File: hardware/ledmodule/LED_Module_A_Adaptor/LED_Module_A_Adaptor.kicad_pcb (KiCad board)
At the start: 4 copper layers, 39.9 x 20.3 mm, 8 parts, among them J1 Conn_LED_Board, J2 Conn_Cable, J3 Conn_01x04, J4 Conn_01x02

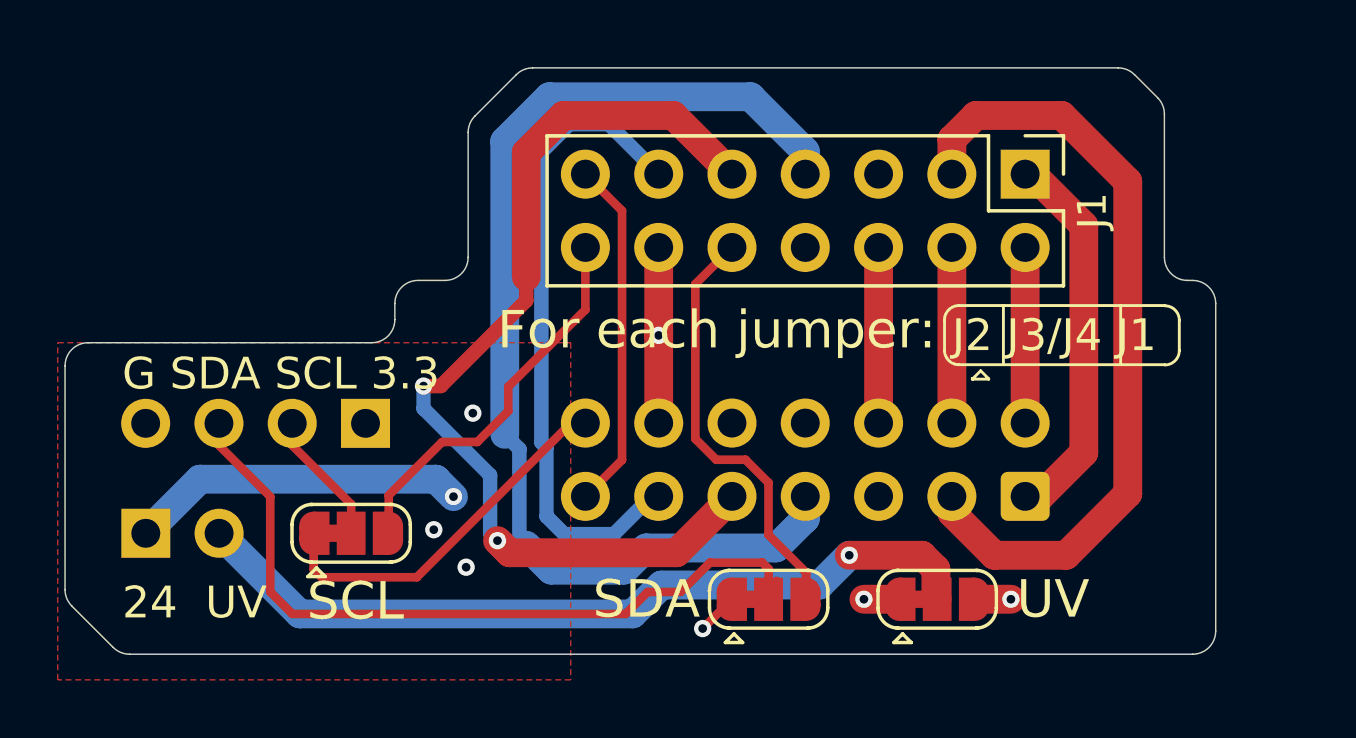
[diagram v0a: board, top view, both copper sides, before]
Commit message: v2 of the adaptor, which now should really fit into the enclosure.
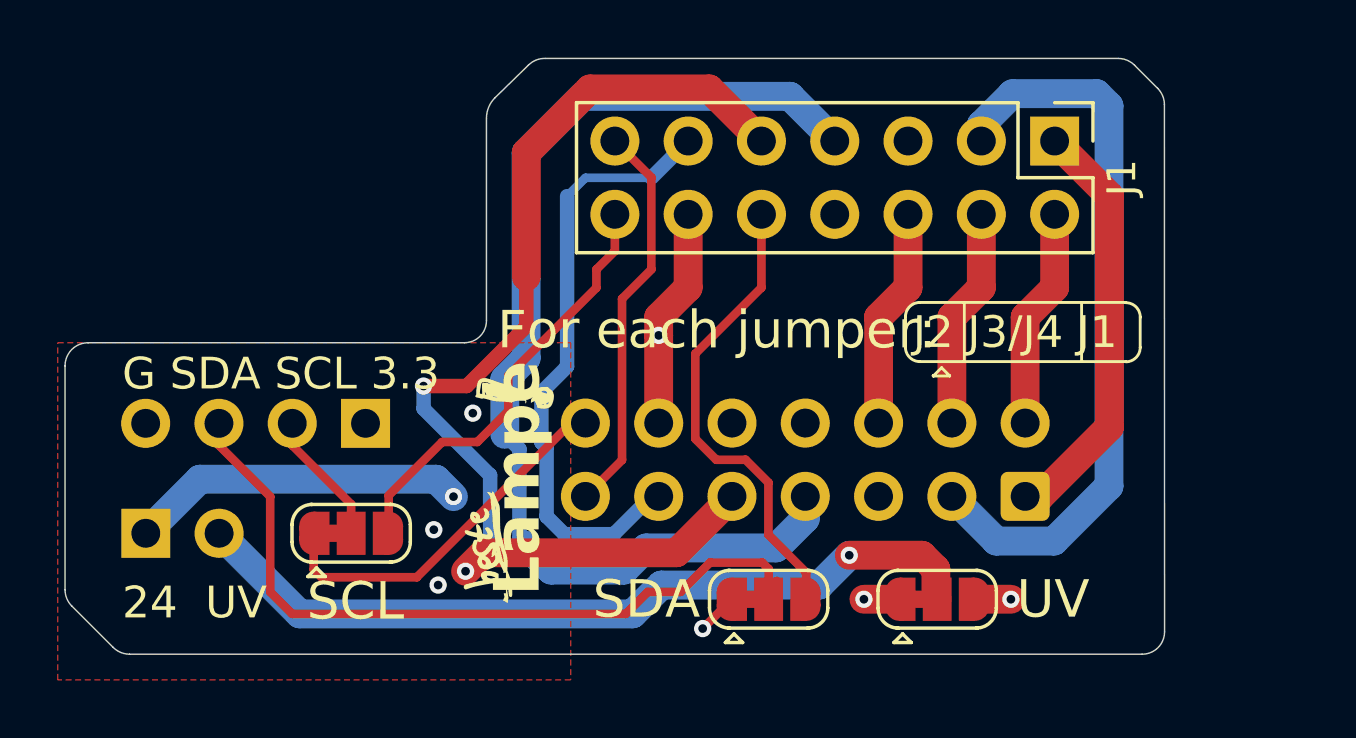
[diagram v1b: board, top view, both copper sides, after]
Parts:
- G***: moved to F.Cu
- moved G*** 23.3 mm to (48.3, 35.4)
- moved J1 1.54 mm to (67.3, 23.5)
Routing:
- net /L0.5_CW: track 34.0 -> 38.3 mm
- net /+3.3V: track 32.0 -> 35.4 mm
- net /L0.2_G: track 27.6 -> 25.7 mm
- net GND: track 49.8 -> 51.5 mm
- net /+5V: track 6.10 -> 7.67 mm
- net /TMP_SCL: track 13.4 -> 15.0 mm
- net /GND_SDA: track 14.9 -> 16.5 mm
- net /+24V: track 35.2 -> 36.8 mm
- net /NEO: track 12.2 -> 13.8 mm
- net /L0.6_A: track 22.9 -> 21.5 mm
- net /L0.1_R: track 13.3 -> 14.6 mm
- net /L0.4_WW: track 38.5 -> 37.9 mm
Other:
- board size 39.9 x 20.3 mm -> 38.1 x 20.6 mm
- board text added: "Adaptor v2 for"
- board text removed: "Adaptor v1 for"
